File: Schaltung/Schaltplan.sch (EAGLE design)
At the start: 48 parts, among them IC1 ATMEGA1284P, IC3 LP 2950(turn_around), Q1 8MHz, Q2 32.786kHz, Q3 BS170, Q4 BS170, Q5 BC547B, Q6 BC557B

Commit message: Schaltung un d Board verandert
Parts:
- added R12, R13, R5: 100k, rcl:R-EU_0207/10
- H1, H2, H3, H4: value MOUNT-HOLE3.3 -> MOUNT-HOLE2.8; device holes:MOUNT-HOLE3.3 -> holes:MOUNT-HOLE2.8
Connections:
- removed net N$26: SD-KARTE.3
- removed net N$27: SD-KARTE.4
- removed net N$28: SD-KARTE.5
- removed net N$29: SD-KARTE.6
- removed net N$30: SD-KARTE.7
- new net CARD-DETECT: IC1.PCINT4/ADC4_PA4, SD-KARTE.7
- net +3V3: now also R5.1
- net BUCHOUT: now also R12.2
- net CS: now also R5.2, SD-KARTE.6
- net GND: now also R12.1
- net MISO: now also SD-KARTE.4
- net MOSI: now also SD-KARTE.3
- net SCK: now also SD-KARTE.5
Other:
- moved on the sheet: H1, H2, H3, H4, L1

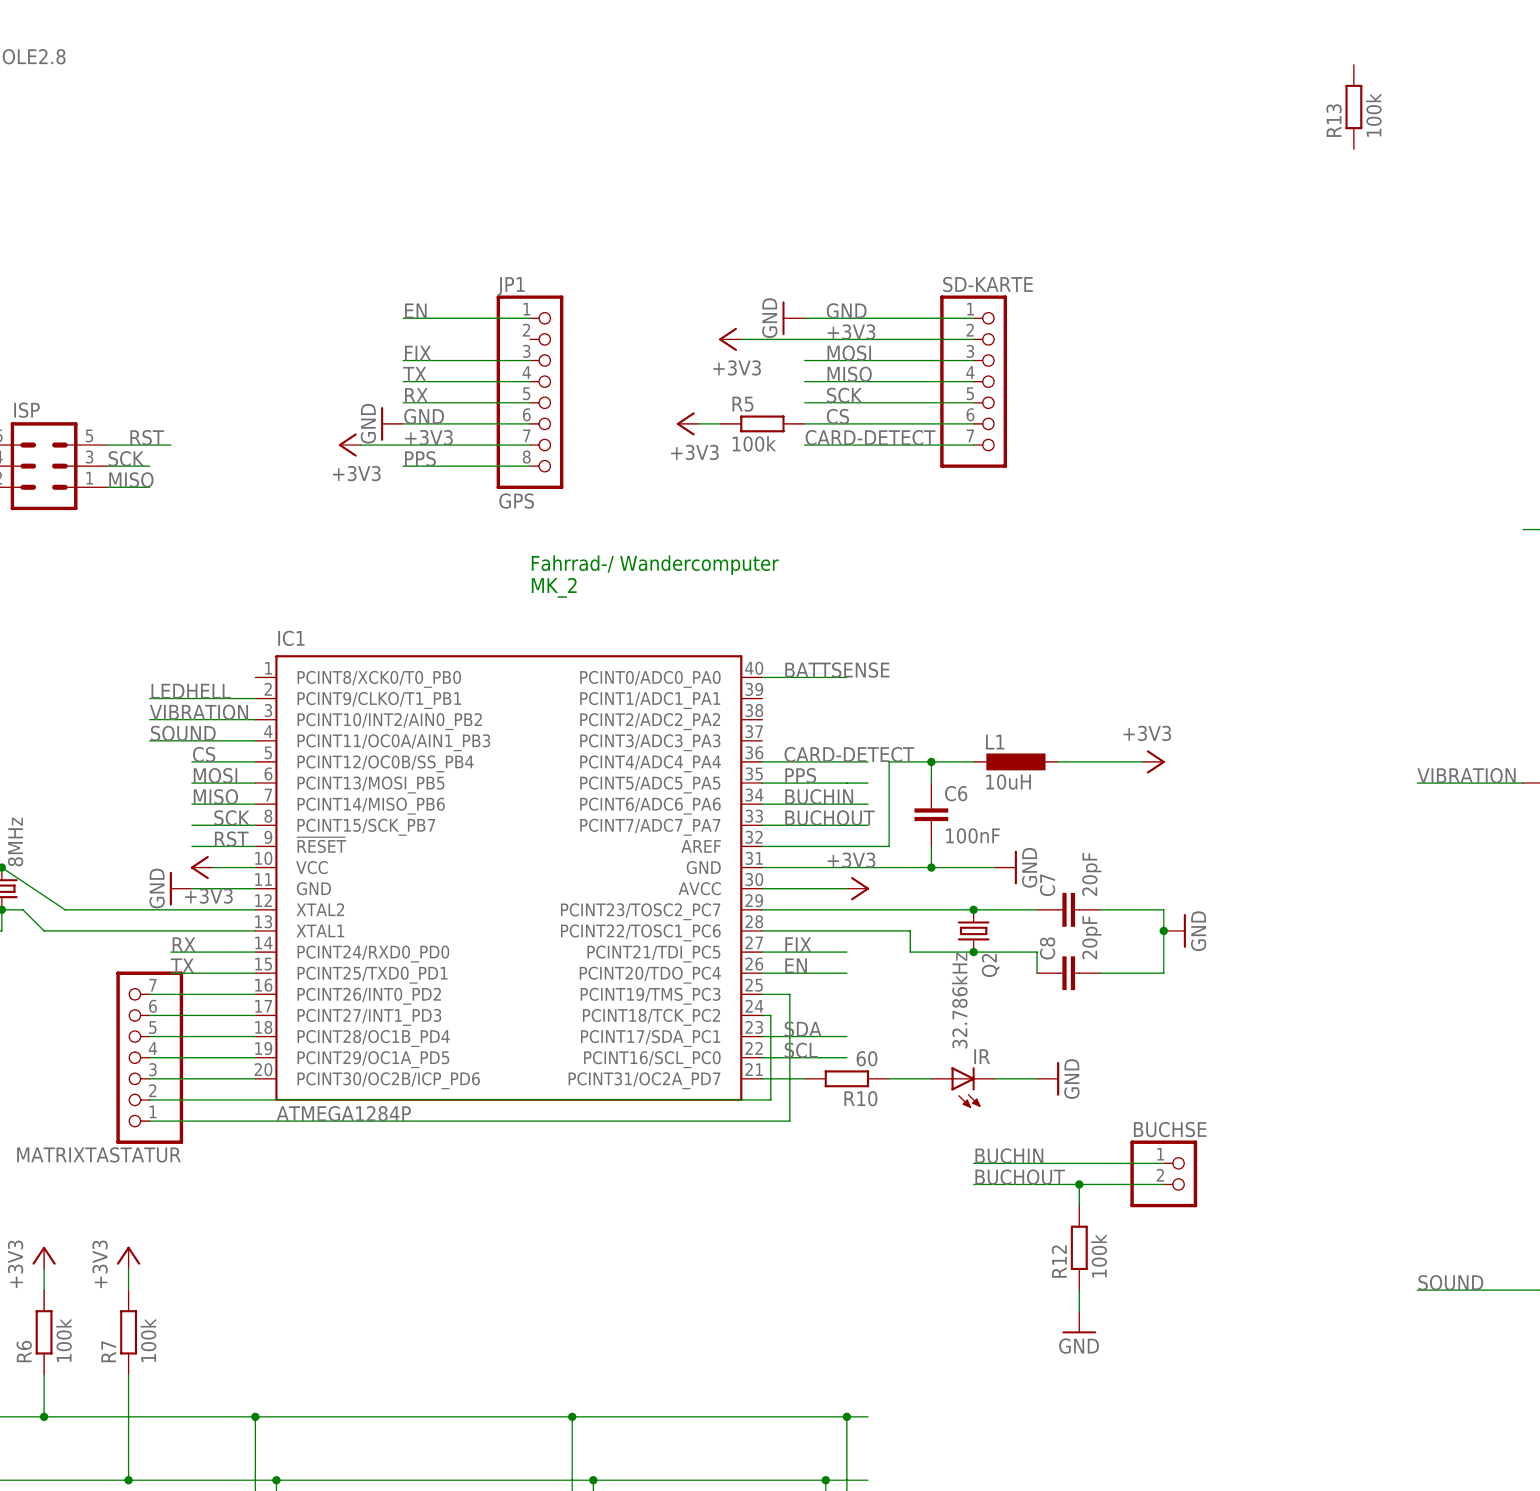
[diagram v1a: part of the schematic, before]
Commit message: Schaltplan/Board beim Hersteller hochgeladen
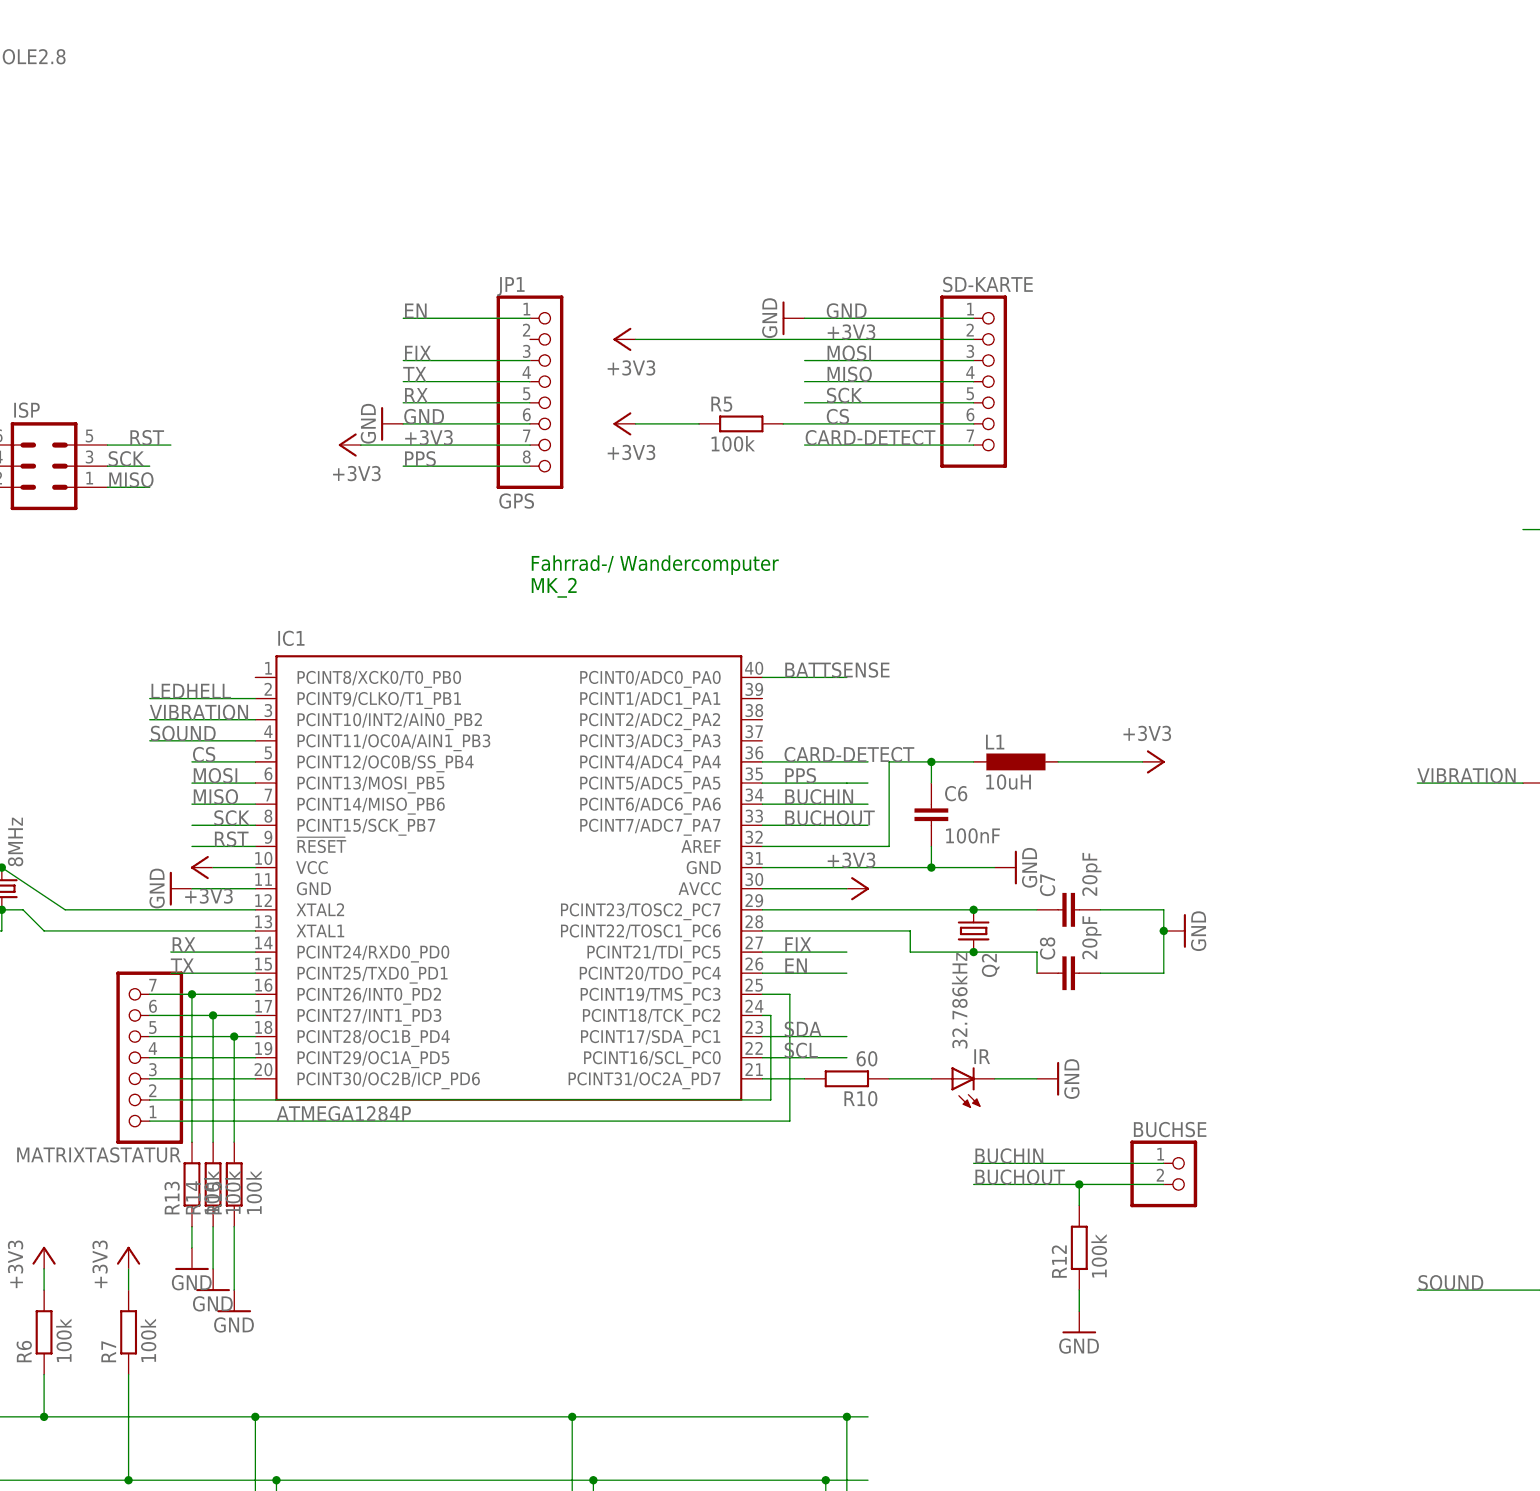
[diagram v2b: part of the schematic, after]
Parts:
- added R14, R15: 100k, rcl:R-EU_0207/10
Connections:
- net GND: now also R13.1, R14.1, R15.1
- net N$11: now also R13.2
- net N$12: now also R14.2
- net N$13: now also R15.2
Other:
- moved on the sheet: R13, R5
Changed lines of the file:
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@@
 <part name="C6" library="rcl" deviceset="C-EU" device="025-024X044" value="100nF"/>
 <part name="R13" library="rcl" deviceset="R-EU_" device="0207/10" value="100k"/>
+<part name="R14" library="rcl" deviceset="R-EU_" device="0207/10" value="100k"/>
+<part name="R15" library="rcl" deviceset="R-EU_" device="0207/10" value="100k"/>
+<part name="GND20" library="supply1" deviceset="GND" device=""/>
+<part name="GND21" library="supply1" deviceset="GND" device=""/>
+<part name="GND22" library="supply1" deviceset="GND" device=""/>
 </parts>
 <sheets>
@@
 <instance part="SD-KARTE" gate="A" x="124.46" y="111.76"/>
 <instance part="GND18" gate="1" x="99.06" y="119.38" rot="R270"/>
-<instance part="+3V16" gate="G$1" x="91.44" y="116.84" rot="R90"/>
-<instance part="R5" gate="G$1" x="96.52" y="106.68"/>
-<instance part="+3V17" gate="G$1" x="86.36" y="106.68" rot="R90"/>
+<instance part="+3V16" gate="G$1" x="78.74" y="116.84" rot="R90"/>
+<instance part="R5" gate="G$1" x="93.98" y="106.68"/>
+<instance part="+3V17" gate="G$1" x="78.74" y="106.68" rot="R90"/>
 <instance part="H1" gate="G$1" x="-76.2" y="152.4"/>
 <instance part="H2" gate="G$1" x="-53.34" y="152.4"/>
@@
 <instance part="R12" gate="G$1" x="134.62" y="7.62" rot="R90"/>
 <instance part="C6" gate="G$1" x="116.84" y="60.96"/>
-<instance part="R13" gate="G$1" x="167.64" y="144.78" rot="R90"/>
+<instance part="R13" gate="G$1" x="27.94" y="15.24" rot="R90"/>
+<instance part="R14" gate="G$1" x="30.48" y="15.24" rot="R90"/>
+<instance part="R15" gate="G$1" x="33.02" y="15.24" rot="R90"/>
+<instance part="GND20" gate="1" x="27.94" y="5.08"/>
+<instance part="GND21" gate="1" x="30.48" y="2.54"/>
+<instance part="GND22" gate="1" x="33.02" y="0"/>
 </instances>
 <busses>
@@
 <junction x="-68.58" y="68.58"/>
 </segment>
+<segment>
+<pinref part="R13" gate="G$1" pin="1"/>
+<pinref part="GND20" gate="1" pin="GND"/>
+<wire x1="27.94" y1="10.16" x2="27.94" y2="7.62" width="0.1524" layer="91"/>
+</segment>
+<segment>
+<pinref part="R14" gate="G$1" pin="1"/>
+<pinref part="GND21" gate="1" pin="GND"/>
+<wire x1="30.48" y1="10.16" x2="30.48" y2="5.08" width="0.1524" layer="91"/>
+</segment>
+<segment>
+<pinref part="R15" gate="G$1" pin="1"/>
+<pinref part="GND22" gate="1" pin="GND"/>
+<wire x1="33.02" y1="10.16" x2="33.02" y2="2.54" width="0.1524" layer="91"/>
+</segment>
 </net>
 <net name="+3V3" class="0">
@@
 <segment>
 <pinref part="SD-KARTE" gate="A" pin="2"/>
-<wire x1="121.92" y1="116.84" x2="93.98" y2="116.84" width="0.1524" layer="91"/>
+<wire x1="121.92" y1="116.84" x2="81.28" y2="116.84" width="0.1524" layer="91"/>
 <label x="104.14" y="116.84" size="1.778" layer="95"/>
 <pinref part="+3V16" gate="G$1" pin="+3V3"/>
@@
 <pinref part="R5" gate="G$1" pin="1"/>
 <pinref part="+3V17" gate="G$1" pin="+3V3"/>
-<wire x1="88.9" y1="106.68" x2="91.44" y2="106.68" width="0.1524" layer="91"/>
+<wire x1="81.28" y1="106.68" x2="88.9" y2="106.68" width="0.1524" layer="91"/>
 </segment>
 </net>
@@
 <segment>
 <pinref part="SD-KARTE" gate="A" pin="6"/>
-<wire x1="121.92" y1="106.68" x2="101.6" y2="106.68" width="0.1524" layer="91"/>
+<wire x1="121.92" y1="106.68" x2="99.06" y2="106.68" width="0.1524" layer="91"/>
 <label x="104.14" y="106.68" size="1.778" layer="95"/>
 <pinref part="R5" gate="G$1" pin="2"/>
@@
 </segment>
 </net>
-<net name="N$11" class="0">
-<segment>
-<pinref part="MATRIXTASTATUR" gate="A" pin="7"/>
-<pinref part="IC1" gate="G$1" pin="PCINT26/INT0_PD2"/>
-<wire x1="22.86" y1="38.1" x2="35.56" y2="38.1" width="0.1524" layer="91"/>
-</segment>
-</net>
-<net name="N$12" class="0">
-<segment>
-<pinref part="IC1" gate="G$1" pin="PCINT27/INT1_PD3"/>
-<pinref part="MATRIXTASTATUR" gate="A" pin="6"/>
-<wire x1="35.56" y1="35.56" x2="22.86" y2="35.56" width="0.1524" layer="91"/>
-</segment>
-</net>
-<net name="N$13" class="0">
-<segment>
-<pinref part="MATRIXTASTATUR" gate="A" pin="5"/>
-<pinref part="IC1" gate="G$1" pin="PCINT28/OC1B_PD4"/>
-<wire x1="22.86" y1="33.02" x2="35.56" y2="33.02" width="0.1524" layer="91"/>
-</segment>
-</net>
-<net name="N$15" class="0">
-<segment>
-<pinref part="MATRIXTASTATUR" gate="A" pin="4"/>
-<pinref part="IC1" gate="G$1" pin="PCINT29/OC1A_PD5"/>
-<wire x1="22.86" y1="30.48" x2="35.56" y2="30.48" width="0.1524" layer="91"/>
-</segment>
-</net>
 <net name="N$16" class="0">
 <segment>
@@
 </segment>
 </net>
+<net name="N$15" class="0">
+<segment>
+<pinref part="IC1" gate="G$1" pin="PCINT29/OC1A_PD5"/>
+<pinref part="MATRIXTASTATUR" gate="A" pin="4"/>
+<wire x1="35.56" y1="30.48" x2="22.86" y2="30.48" width="0.1524" layer="91"/>
+</segment>
+</net>
+<net name="N$11" class="0">
+<segment>
+<pinref part="MATRIXTASTATUR" gate="A" pin="7"/>
+<pinref part="IC1" gate="G$1" pin="PCINT26/INT0_PD2"/>
+<wire x1="22.86" y1="38.1" x2="27.94" y2="38.1" width="0.1524" layer="91"/>
+<pinref part="R13" gate="G$1" pin="2"/>
+<wire x1="27.94" y1="38.1" x2="35.56" y2="38.1" width="0.1524" layer="91"/>
+<wire x1="27.94" y1="20.32" x2="27.94" y2="38.1" width="0.1524" layer="91"/>
+<junction x="27.94" y="38.1"/>
+</segment>
+</net>
+<net name="N$12" class="0">
+<segment>
+<pinref part="IC1" gate="G$1" pin="PCINT27/INT1_PD3"/>
+<pinref part="MATRIXTASTATUR" gate="A" pin="6"/>
+<wire x1="35.56" y1="35.56" x2="30.48" y2="35.56" width="0.1524" layer="91"/>
+<pinref part="R14" gate="G$1" pin="2"/>
+<wire x1="30.48" y1="35.56" x2="22.86" y2="35.56" width="0.1524" layer="91"/>
+<wire x1="30.48" y1="20.32" x2="30.48" y2="35.56" width="0.1524" layer="91"/>
+<junction x="30.48" y="35.56"/>
+</segment>
+</net>
+<net name="N$13" class="0">
+<segment>
+<pinref part="IC1" gate="G$1" pin="PCINT28/OC1B_PD4"/>
+<pinref part="MATRIXTASTATUR" gate="A" pin="5"/>
+<wire x1="35.56" y1="33.02" x2="33.02" y2="33.02" width="0.1524" layer="91"/>
+<pinref part="R15" gate="G$1" pin="2"/>
+<wire x1="33.02" y1="33.02" x2="22.86" y2="33.02" width="0.1524" layer="91"/>
+<wire x1="33.02" y1="20.32" x2="33.02" y2="33.02" width="0.1524" layer="91"/>
+<junction x="33.02" y="33.02"/>
+</segment>
+</net>
